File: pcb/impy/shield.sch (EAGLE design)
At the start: 116 parts, among them J1 USB-2410-06, J2 SI-60062-F, J3 5V, U1 AD5933YRS, U10 LTC3406AB, U11 23LCV1024-I/SN, U12 MIC2009A-1YM6, U13 ADG725BSU, U14 ADG725BSU, U2 ADG704BRM, U3 AD8656ARZ, U4 M24C08WMN, U5 ADG706BRU, U6 DP83848I, U7 MIC2009A-1YM6, U8 AT25DF081A-SS, U9 SST25VF080B-80-4I-S2

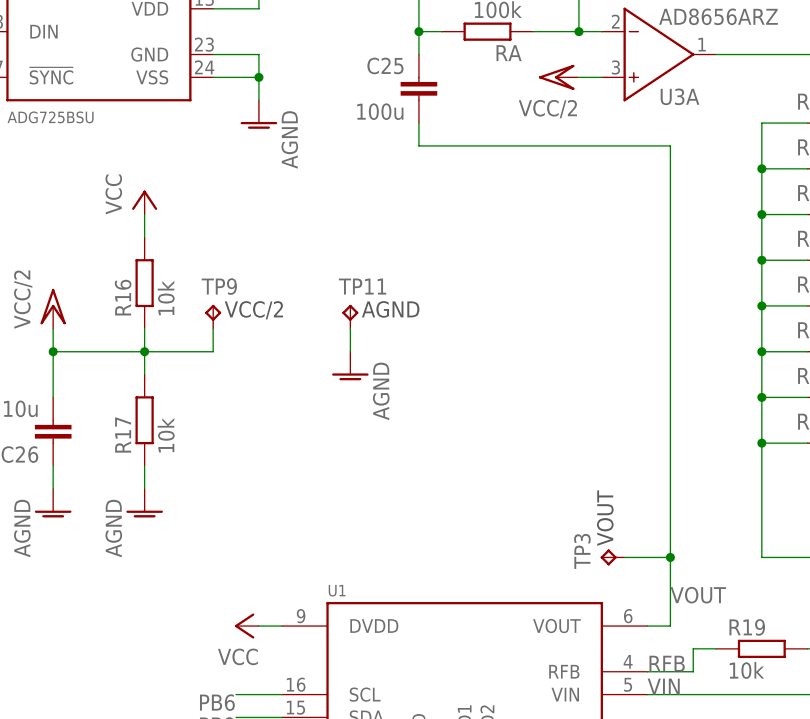
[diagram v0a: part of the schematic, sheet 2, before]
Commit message: * pcb/impy: (shield.sch, shield.brd) Add output GND connectors and resize board to fit them.
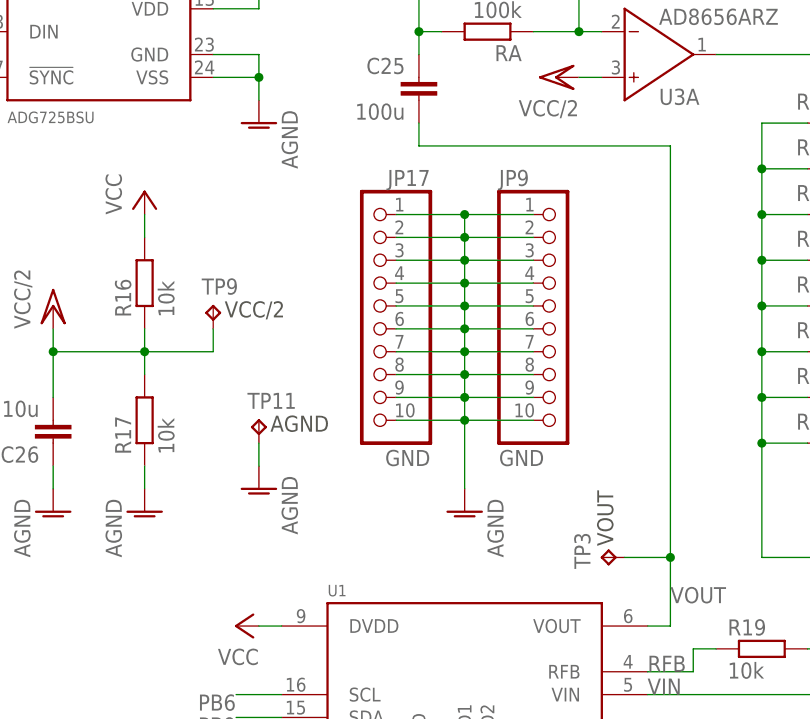
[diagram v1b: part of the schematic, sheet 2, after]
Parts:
- added JP17, JP9: GND, pinhead:PINHD-1X10
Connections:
- net AGND: now also JP17.1, JP17.10, JP17.2, JP17.3, JP17.4, JP17.5, JP17.6, JP17.7, JP17.8, JP17.9, JP9.1, JP9.10, JP9.2, JP9.3, JP9.4, JP9.5, JP9.6, JP9.7, JP9.8, JP9.9
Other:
- moved on the sheet: TP11
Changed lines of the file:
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@@
 <part name="GND45" library="supply1" deviceset="GND" device=""/>
 <part name="AGND15" library="supply1" deviceset="AGND" device=""/>
+<part name="JP9" library="pinhead" deviceset="PINHD-1X10" device="" value="GND"/>
+<part name="JP17" library="pinhead" deviceset="PINHD-1X10" device="" value="GND"/>
+<part name="AGND16" library="supply1" deviceset="AGND" device=""/>
 </parts>
 <sheets>
@@
 <instance part="TP9" gate="G$1" x="20.32" y="88.9"/>
 <instance part="TP10" gate="G$1" x="43.18" y="127"/>
-<instance part="TP11" gate="G$1" x="35.56" y="88.9"/>
-<instance part="AGND14" gate="VR1" x="35.56" y="81.28" rot="MR0"/>
+<instance part="TP11" gate="G$1" x="25.4" y="76.2"/>
+<instance part="AGND14" gate="VR1" x="25.4" y="68.58" rot="MR0"/>
 <instance part="AGND15" gate="VR1" x="111.76" y="53.34" smashed="yes">
 <attribute name="VALUE" x="111.76" y="55.88" size="1.778" layer="96" rot="R180"/>
 </instance>
+<instance part="JP9" gate="A" x="58.42" y="88.9" smashed="yes">
+<attribute name="NAME" x="52.07" y="102.235" size="1.778" layer="95"/>
+<attribute name="VALUE" x="52.07" y="71.12" size="1.778" layer="96"/>
+</instance>
+<instance part="JP17" gate="A" x="38.1" y="88.9" smashed="yes" rot="MR0">
+<attribute name="NAME" x="44.45" y="102.235" size="1.778" layer="95" rot="MR0"/>
+<attribute name="VALUE" x="44.45" y="71.12" size="1.778" layer="96" rot="MR0"/>
+</instance>
+<instance part="AGND16" gate="VR1" x="48.26" y="66.04" rot="MR0"/>
 </instances>
 <busses>
@@
 <pinref part="AGND14" gate="VR1" pin="AGND"/>
 <pinref part="TP11" gate="G$1" pin="TP"/>
-<wire x1="35.56" y1="83.82" x2="35.56" y2="86.36" width="0.1524" layer="91"/>
+<wire x1="25.4" y1="71.12" x2="25.4" y2="73.66" width="0.1524" layer="91"/>
 </segment>
 <segment>
@@
 <wire x1="111.76" y1="58.42" x2="111.76" y2="55.88" width="0.1524" layer="91"/>
 </segment>
-</net>
+<segment>
+<pinref part="JP9" gate="A" pin="1"/>
+<pinref part="JP17" gate="A" pin="1"/>
+<wire x1="40.64" y1="99.06" x2="48.26" y2="99.06" width="0.1524" layer="91"/>
+<pinref part="JP9" gate="A" pin="2"/>
+<pinref part="JP17" gate="A" pin="2"/>
+<wire x1="48.26" y1="99.06" x2="55.88" y2="99.06" width="0.1524" layer="91"/>
+<wire x1="40.64" y1="96.52" x2="48.26" y2="96.52" width="0.1524" layer="91"/>
+<wire x1="48.26" y1="96.52" x2="55.88" y2="96.52" width="0.1524" layer="91"/>
+<wire x1="48.26" y1="99.06" x2="48.26" y2="96.52" width="0.1524" layer="91"/>
+<junction x="48.26" y="99.06"/>
+<junction x="48.26" y="96.52"/>
+<pinref part="JP9" gate="A" pin="3"/>
+<pinref part="JP17" gate="A" pin="3"/>
+<wire x1="40.64" y1="93.98" x2="48.26" y2="93.98" width="0.1524" layer="91"/>
+<wire x1="48.26" y1="93.98" x2="55.88" y2="93.98" width="0.1524" layer="91"/>
+<wire x1="48.26" y1="96.52" x2="48.26" y2="93.98" width="0.1524" layer="91"/>
+<junction x="48.26" y="93.98"/>
+<pinref part="JP9" gate="A" pin="4"/>
+<pinref part="JP17" gate="A" pin="4"/>
+<wire x1="40.64" y1="91.44" x2="48.26" y2="91.44" width="0.1524" layer="91"/>
+<wire x1="48.26" y1="91.44" x2="55.88" y2="91.44" width="0.1524" layer="91"/>
+<wire x1="48.26" y1="93.98" x2="48.26" y2="91.44" width="0.1524" layer="91"/>
+<junction x="48.26" y="91.44"/>
+<pinref part="JP9" gate="A" pin="5"/>
+<pinref part="JP17" gate="A" pin="5"/>
+<wire x1="40.64" y1="88.9" x2="48.26" y2="88.9" width="0.1524" layer="91"/>
+<wire x1="48.26" y1="88.9" x2="55.88" y2="88.9" width="0.1524" layer="91"/>
+<wire x1="48.26" y1="91.44" x2="48.26" y2="88.9" width="0.1524" layer="91"/>
+<junction x="48.26" y="88.9"/>
+<pinref part="JP9" gate="A" pin="6"/>
+<pinref part="JP17" gate="A" pin="6"/>
+<wire x1="40.64" y1="86.36" x2="48.26" y2="86.36" width="0.1524" layer="91"/>
+<wire x1="48.26" y1="86.36" x2="55.88" y2="86.36" width="0.1524" layer="91"/>
+<wire x1="48.26" y1="88.9" x2="48.26" y2="86.36" width="0.1524" layer="91"/>
+<junction x="48.26" y="86.36"/>
+<pinref part="JP9" gate="A" pin="7"/>
+<pinref part="JP17" gate="A" pin="7"/>
+<wire x1="40.64" y1="83.82" x2="48.26" y2="83.82" width="0.1524" layer="91"/>
+<wire x1="48.26" y1="83.82" x2="55.88" y2="83.82" width="0.1524" layer="91"/>
+<wire x1="48.26" y1="86.36" x2="48.26" y2="83.82" width="0.1524" layer="91"/>
+<junction x="48.26" y="83.82"/>
+<pinref part="JP9" gate="A" pin="8"/>
+<pinref part="JP17" gate="A" pin="8"/>
+<wire x1="40.64" y1="81.28" x2="48.26" y2="81.28" width="0.1524" layer="91"/>
+<wire x1="48.26" y1="81.28" x2="55.88" y2="81.28" width="0.1524" layer="91"/>
+<wire x1="48.26" y1="83.82" x2="48.26" y2="81.28" width="0.1524" layer="91"/>
+<junction x="48.26" y="81.28"/>
+<pinref part="JP9" gate="A" pin="9"/>
+<pinref part="JP17" gate="A" pin="9"/>
+<wire x1="40.64" y1="78.74" x2="48.26" y2="78.74" width="0.1524" layer="91"/>
+<wire x1="48.26" y1="78.74" x2="55.88" y2="78.74" width="0.1524" layer="91"/>
+<wire x1="48.26" y1="81.28" x2="48.26" y2="78.74" width="0.1524" layer="91"/>
+<junction x="48.26" y="78.74"/>
+<pinref part="JP9" gate="A" pin="10"/>
+<pinref part="JP17" gate="A" pin="10"/>
+<wire x1="40.64" y1="76.2" x2="48.26" y2="76.2" width="0.1524" layer="91"/>
+<wire x1="48.26" y1="76.2" x2="55.88" y2="76.2" width="0.1524" layer="91"/>
+<wire x1="48.26" y1="78.74" x2="48.26" y2="76.2" width="0.1524" layer="91"/>
+<junction x="48.26" y="76.2"/>
+<pinref part="AGND16" gate="VR1" pin="AGND"/>
+<wire x1="48.26" y1="76.2" x2="48.26" y2="68.58" width="0.1524" layer="91"/>
+</segment>
+</net>

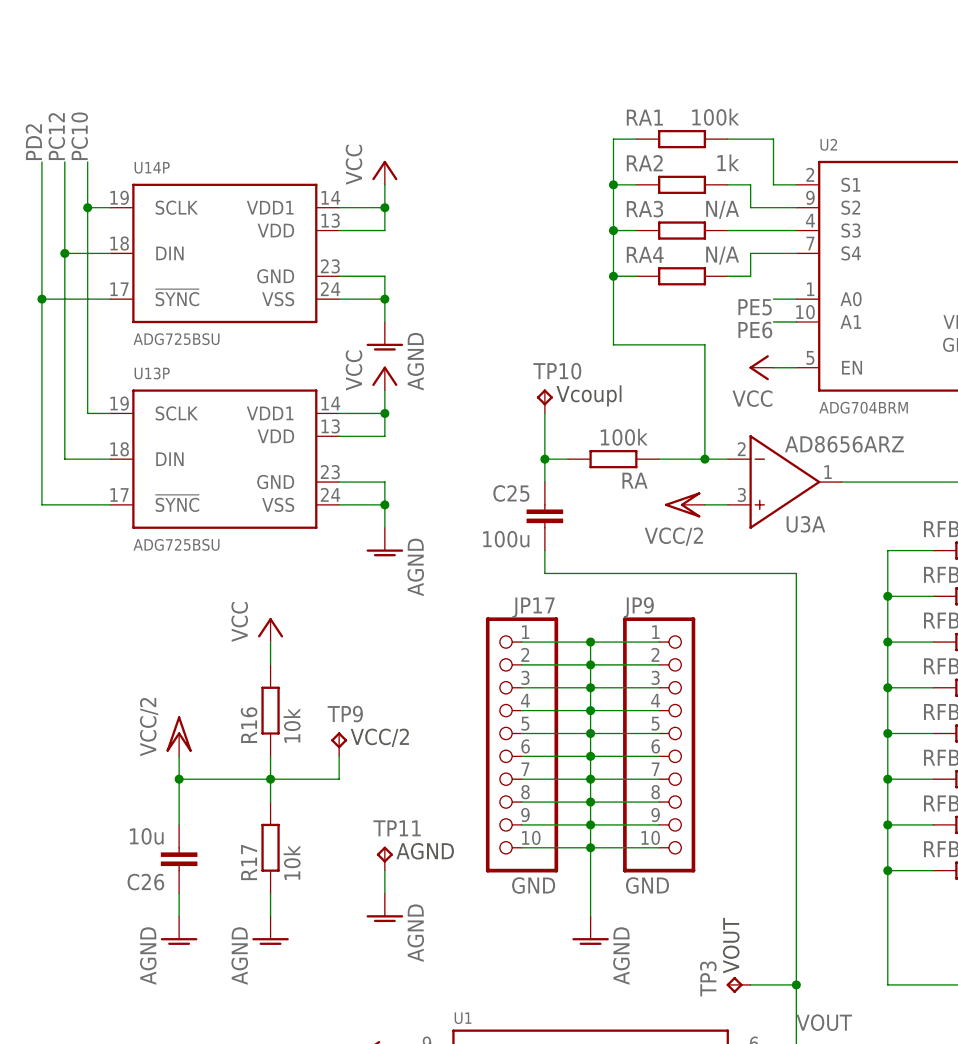
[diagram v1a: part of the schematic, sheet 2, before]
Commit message: * pcb/impy: (shield.sch) Add analog switch to quickly charge the AD5933 output coupling capacitor. Change feedback resistor values for output attenuator and VCC/2 divider.   (shield.brd) Change package size of the coupling capacitor. Layout new components and approve some DRC errors.
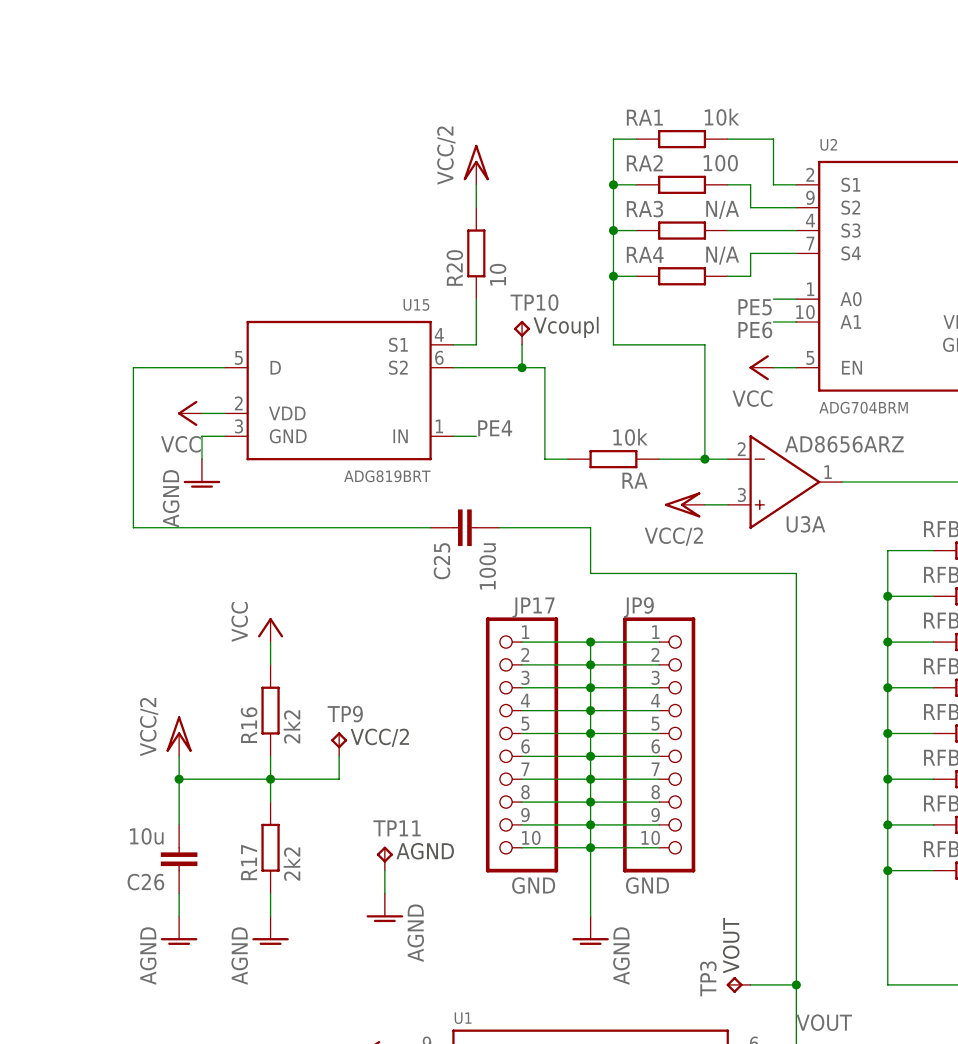
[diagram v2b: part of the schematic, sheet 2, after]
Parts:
- added R20: 10, rcl:R-EU_R0603
- added U15: ADG819BRT, parts:ADG819BRT
- C25: device rcl:C-EUC0603 -> rcl:C-EUC1206
- R16, R17: value 10k -> 2k2
- RA, RA1: value 100k -> 10k
- RA2: value 1k -> 100
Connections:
- new net N$107: C25.1, U15.D
- new net N$108: R20.1, U15.S1
- new net PE4: JP2.13, U15.IN
- net AGND: now also U15.GND
- net N$2: now also U15.S2; no longer C25.1
- net VCC: now also U15.VDD
- net VCC/2: now also R20.2
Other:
- note added: "Mux supply"
- moved on the sheet: C25, TP10

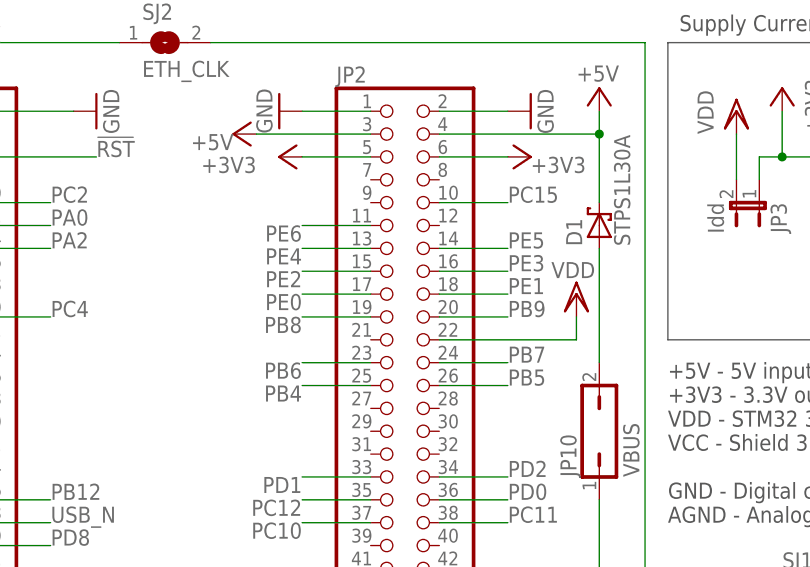
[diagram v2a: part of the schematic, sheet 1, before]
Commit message: * pcb/impy: (shield.sch) Remove unused discovery board connections (PE0, PE1, PE3).
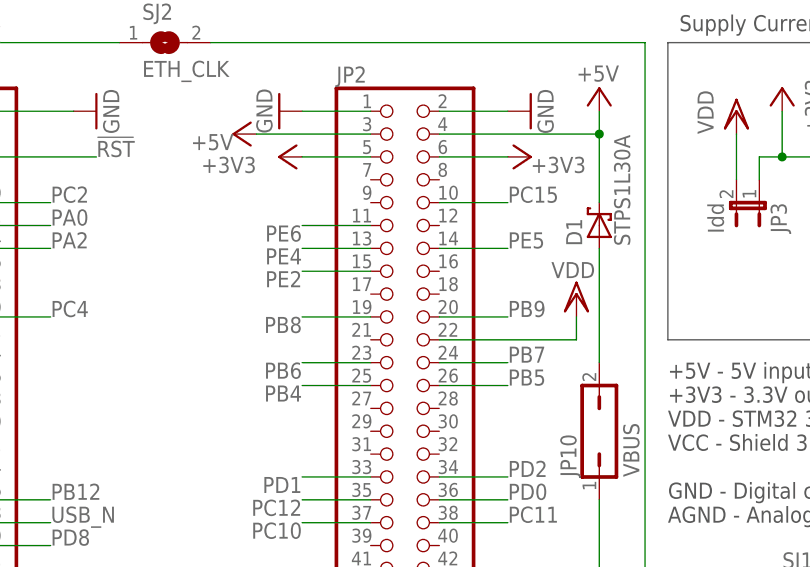
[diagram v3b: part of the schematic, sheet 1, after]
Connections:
- removed net PE0: JP2.17
- removed net PE1: JP2.18
- removed net PE3: JP2.16
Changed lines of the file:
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@@
-</segment>
-</net>
-<net name="PE1" class="0">
-<segment>
-<pinref part="JP2" gate="A" pin="18"/>
-<wire x1="78.74" y1="60.96" x2="86.36" y2="60.96" width="0.1524" layer="91"/>
-<label x="86.36" y="60.96" size="1.778" layer="95"/>
-</segment>
-</net>
-<net name="PE0" class="0">
-<segment>
-<pinref part="JP2" gate="A" pin="17"/>
-<wire x1="71.12" y1="60.96" x2="63.5" y2="60.96" width="0.1524" layer="91"/>
-<label x="63.5" y="60.96" size="1.778" layer="95" rot="R180"/>
-</segment>
-</net>
-<net name="PE3" class="0">
-<segment>
-<pinref part="JP2" gate="A" pin="16"/>
-<wire x1="78.74" y1="63.5" x2="86.36" y2="63.5" width="0.1524" layer="91"/>
-<label x="86.36" y="63.5" size="1.778" layer="95"/>
 </segment>
 </net>

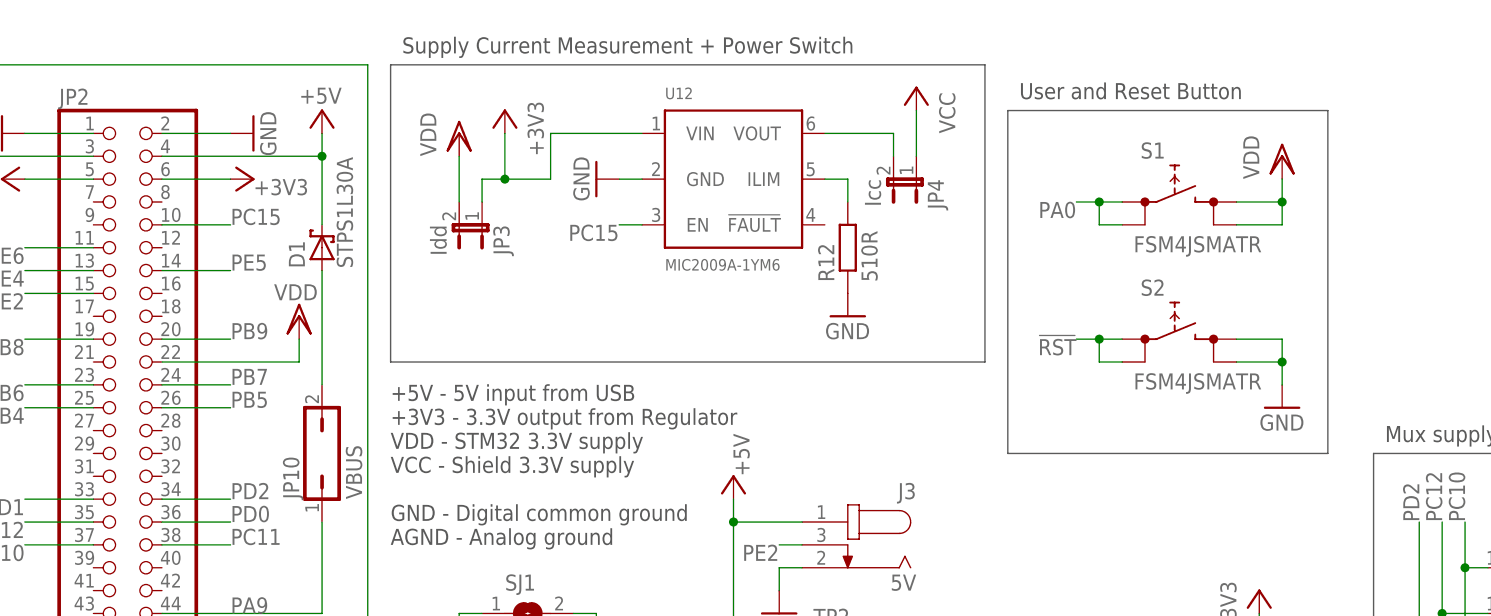
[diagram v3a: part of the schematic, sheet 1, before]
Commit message: * pcb/impy: (shield.sch, shield.brd) Remove peripheral power switch, this doesn't really work without more effort to prevent current from flowing through STM32 pins to the peripherals. Also, it's not really needed.
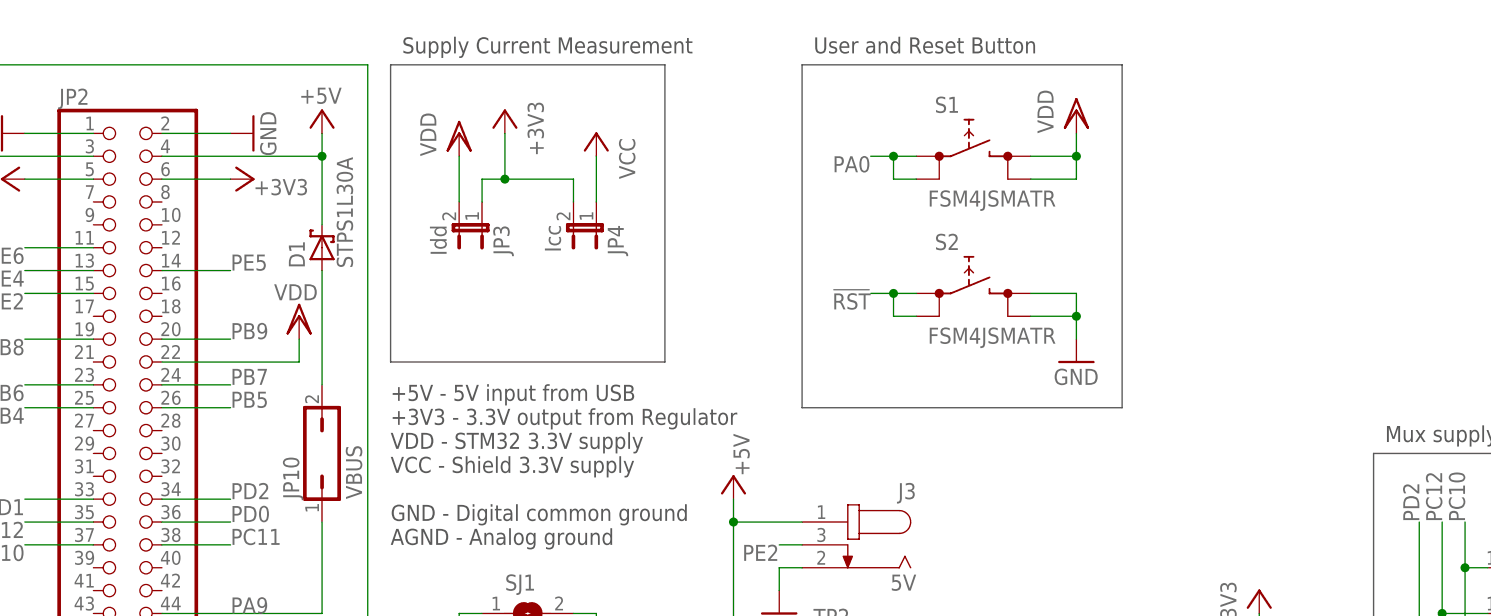
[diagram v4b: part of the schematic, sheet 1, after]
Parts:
- removed R12: 510R, rcl:R-EU_R0603
- removed U12: MIC2009A-1YM6, parts:MIC2009A-1YM6
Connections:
- removed net N$36: JP4.2, U12.VOUT
- removed net N$38: R12.2, U12.ILIM
- removed net PC15: JP2.10, U12.EN
- net +3V3: now also JP4.2; no longer U12.VIN
- net GND: no longer R12.1, U12.GND
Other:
- note added: "Supply Current Measurement"
- note removed: "Supply Current Measurement + Power Switch"
- moved on the sheet: JP4, S1, S2

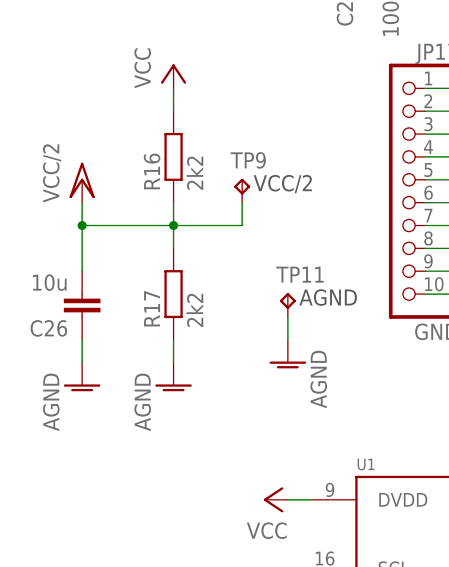
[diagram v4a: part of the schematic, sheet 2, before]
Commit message: * pcb/impy: (shield.sch) Change value of VCC/2 bypass capacitor, this can't be large because it represents a large load to the AD5933 output during coupling capacitor charging.
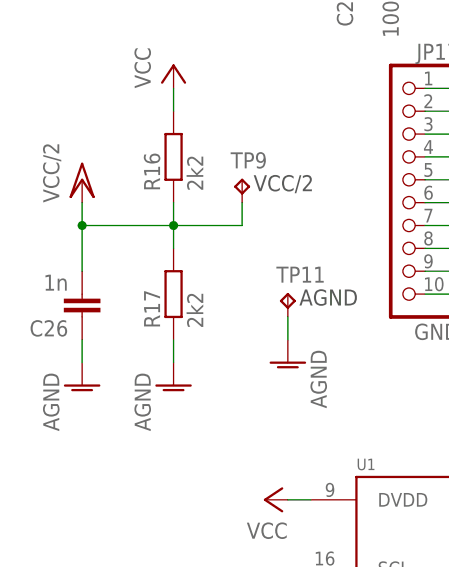
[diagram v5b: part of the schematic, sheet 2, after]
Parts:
- C26: value 10u -> 1n
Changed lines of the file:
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@@
 <part name="R16" library="rcl" deviceset="R-EU_" device="R0603" value="2k2"/>
 <part name="R17" library="rcl" deviceset="R-EU_" device="R0603" value="2k2"/>
-<part name="C26" library="rcl" deviceset="C-EU" device="C0603" value="10u"/>
+<part name="C26" library="rcl" deviceset="C-EU" device="C0603" value="1n"/>
 <part name="AGND4" library="supply1" deviceset="AGND" device=""/>
 <part name="AGND5" library="supply1" deviceset="AGND" device=""/>
